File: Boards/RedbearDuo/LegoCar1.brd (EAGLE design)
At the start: 100 x 100 mm, 89 parts

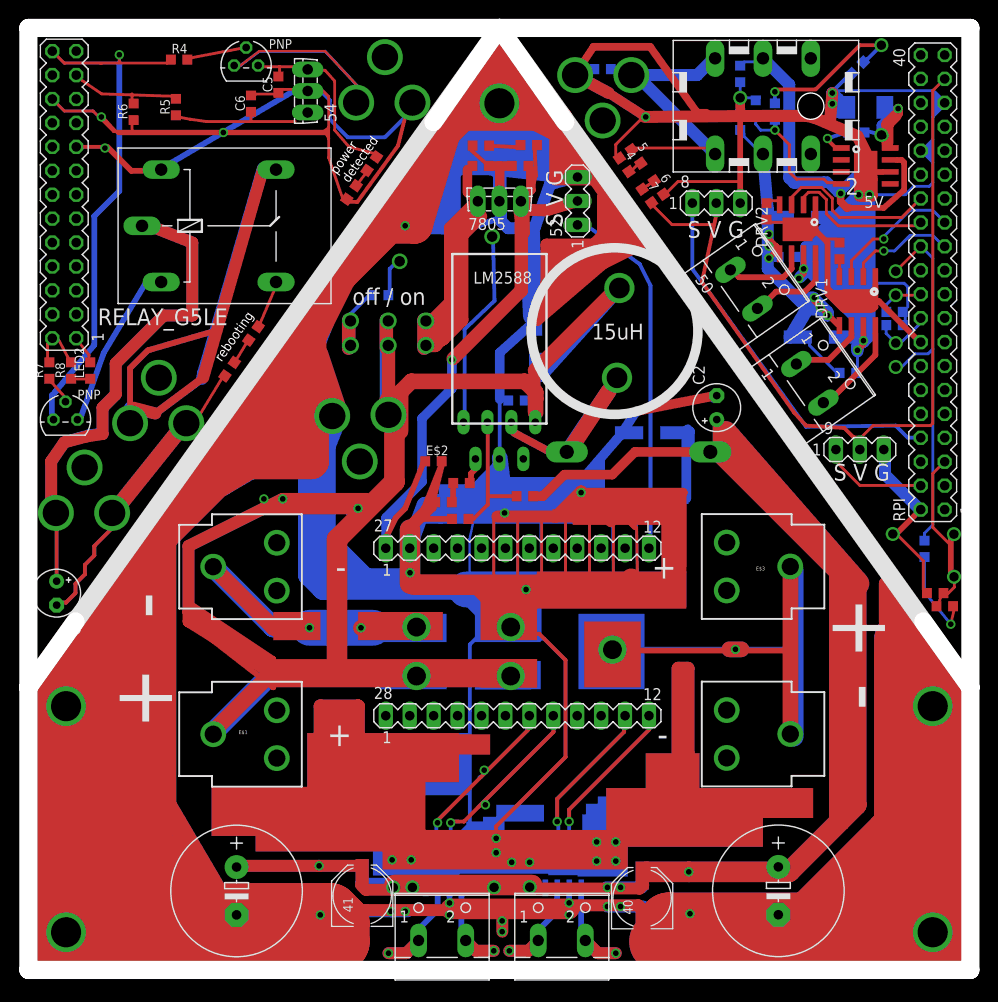
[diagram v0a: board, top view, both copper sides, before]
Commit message: added motor driver library + sample circuit
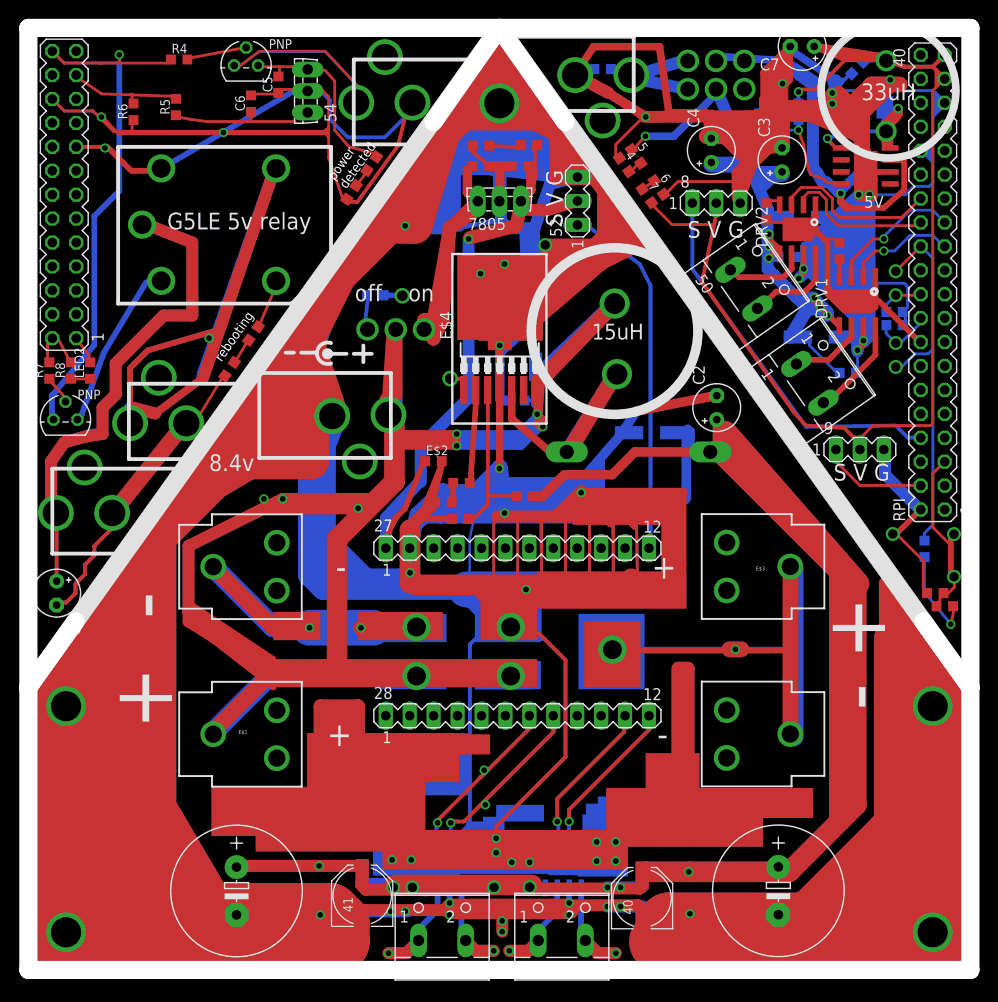
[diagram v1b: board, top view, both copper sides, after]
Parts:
- removed 2: (no value), con-hirschmann:MABSA
- removed LM2588: (no value), infineon:P-TO220-7-11
- removed RELAY_G5LE: (no value), relay:G5LE
- added C3, C4, C7: (no value), rcl:E2,5-5
- added E$4: (no value), led:P-TO263-7-1
- 5V: value (none) -> TPS5410
- moved 1N914 9.60 mm to (42.2, 67.2), turned to 60 degrees
- moved 20 3.04 mm to (78.6, 94.6)
- moved 15 2.55 mm to (79.7, 90.9)
- moved 16 2.50 mm to (81.7, 91.1)
- moved 21 2.00 mm to (77.6, 90.0)
- moved RESISTOR 0.51 mm to (36.8, 71.6)
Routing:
- net S$188: track 50.9 -> 14.9 mm, vias 1 -> 0
- net S$190: track 0.00 -> 31.3 mm, vias 1 -> 0
- net S$352: track 0.00 -> 20.7 mm
- net S$368: track 0.00 -> 20.3 mm
- net S$348: track 0.00 -> 19.5 mm, vias 0 -> 2
- net S$125: track 0.00 -> 17.7 mm
- net S$359: track 0.00 -> 14.5 mm
- net S$340: track 28.0 -> 13.4 mm
- net S$119: track 22.3 -> 7.88 mm, vias 1 -> 0
- net S$117: track 18.3 -> 4.13 mm
- net S$351: track 0.00 -> 13.4 mm
- net S$355: track 0.00 -> 13.0 mm, vias 0 -> 1
- net S$363: track 0.00 -> 12.1 mm
- net S$371: track 0.00 -> 12.0 mm
- net S$370: track 0.00 -> 11.9 mm
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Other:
- board text added: "33uH"
- board text added: "8.4v"
- board text added: "G5LE 5v relay"
- board text added: "off on"
- board text removed: "off / on"
